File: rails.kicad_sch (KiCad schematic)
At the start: 96 parts, among them Q15 2N7002, U13 LM61460AASQRJRRQ1, U14 LM61460AASQRJRRQ1, U15 TPS259474ARPWR, U16 SN74LVC1G74, Y2 SX1M4.000M10F30TNN

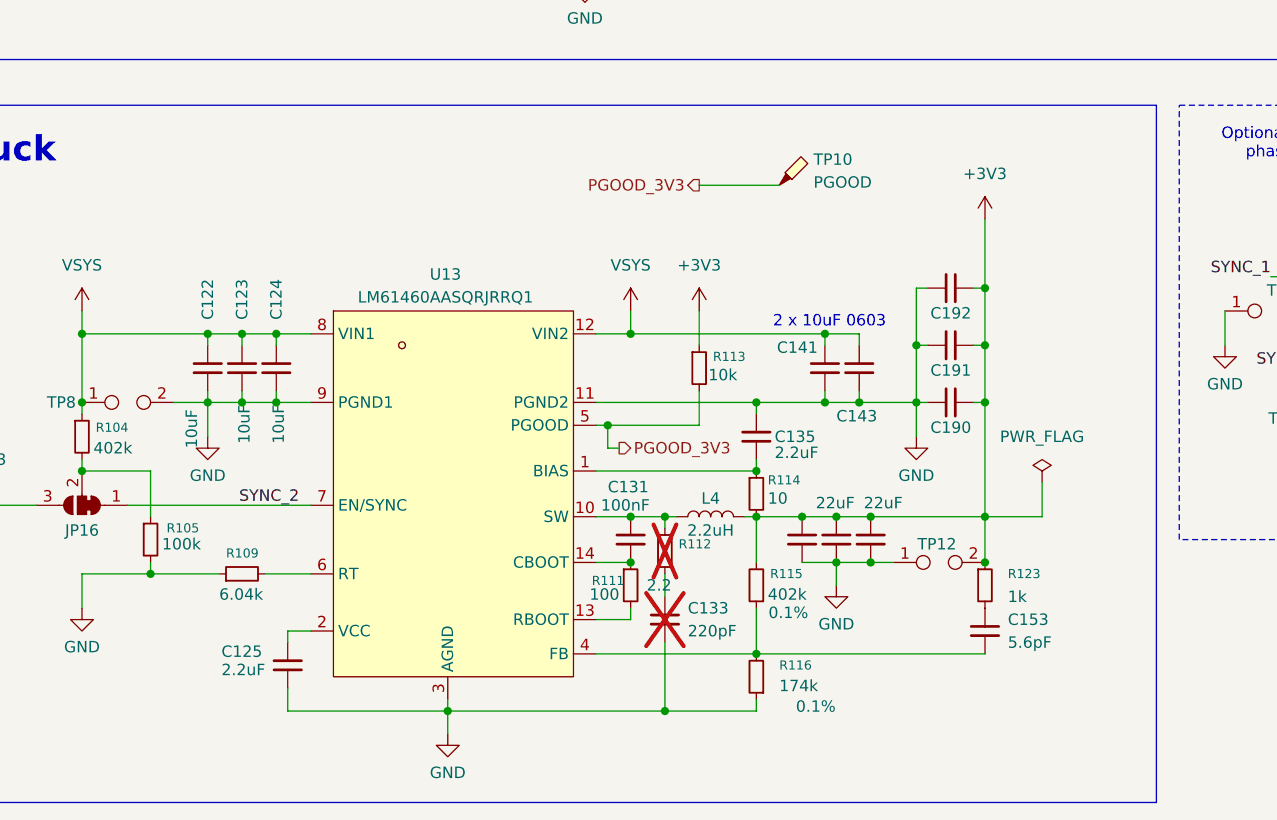
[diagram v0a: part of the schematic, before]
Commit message: checkpoint: schematic WIP before battery -> charger rename
Connectors and Overview sheets, LSM6DSV16X/TPS22945/charger datasheets,
and in-progress edits across all sheets, committed as-is so the rename
diff stands alone.

Co-Authored-By: Claude Opus 5.5 <noreply@anthropic.com>
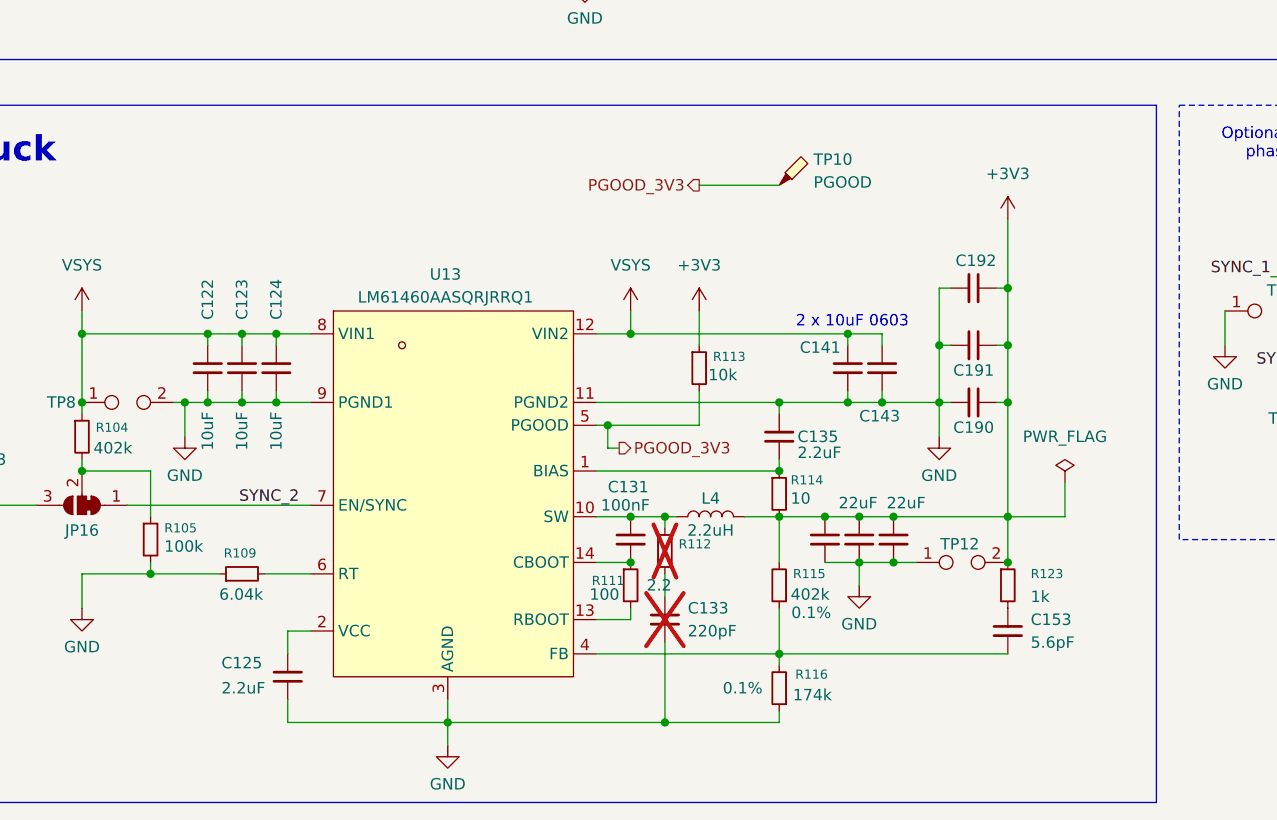
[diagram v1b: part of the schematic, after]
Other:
- title: Power Regulators -> 5 V & 3.3 V Buck Regulators
- moved on the sheet: C125, C135, C141, C143, C153, C190, C191, C192, R114, R115, R116, R123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
